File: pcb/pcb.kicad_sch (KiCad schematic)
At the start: 43 parts, among them J1 GND, J10 SWDIO, J11 SWCLK, J12 USART1 TX, J13 USART1 RX, J14 VDD, J2 +3.3V, J3 LCD Data, J4 LCD RS, J5 LCD E, J6 3.3v, J7 ADC2, J8 GND, J9 USART3 TX, P1 USB_C_Plug_USB2.0, U1 TLV62569DBV, U2 STM32F446RETx, U3 MCP73831-2-OT

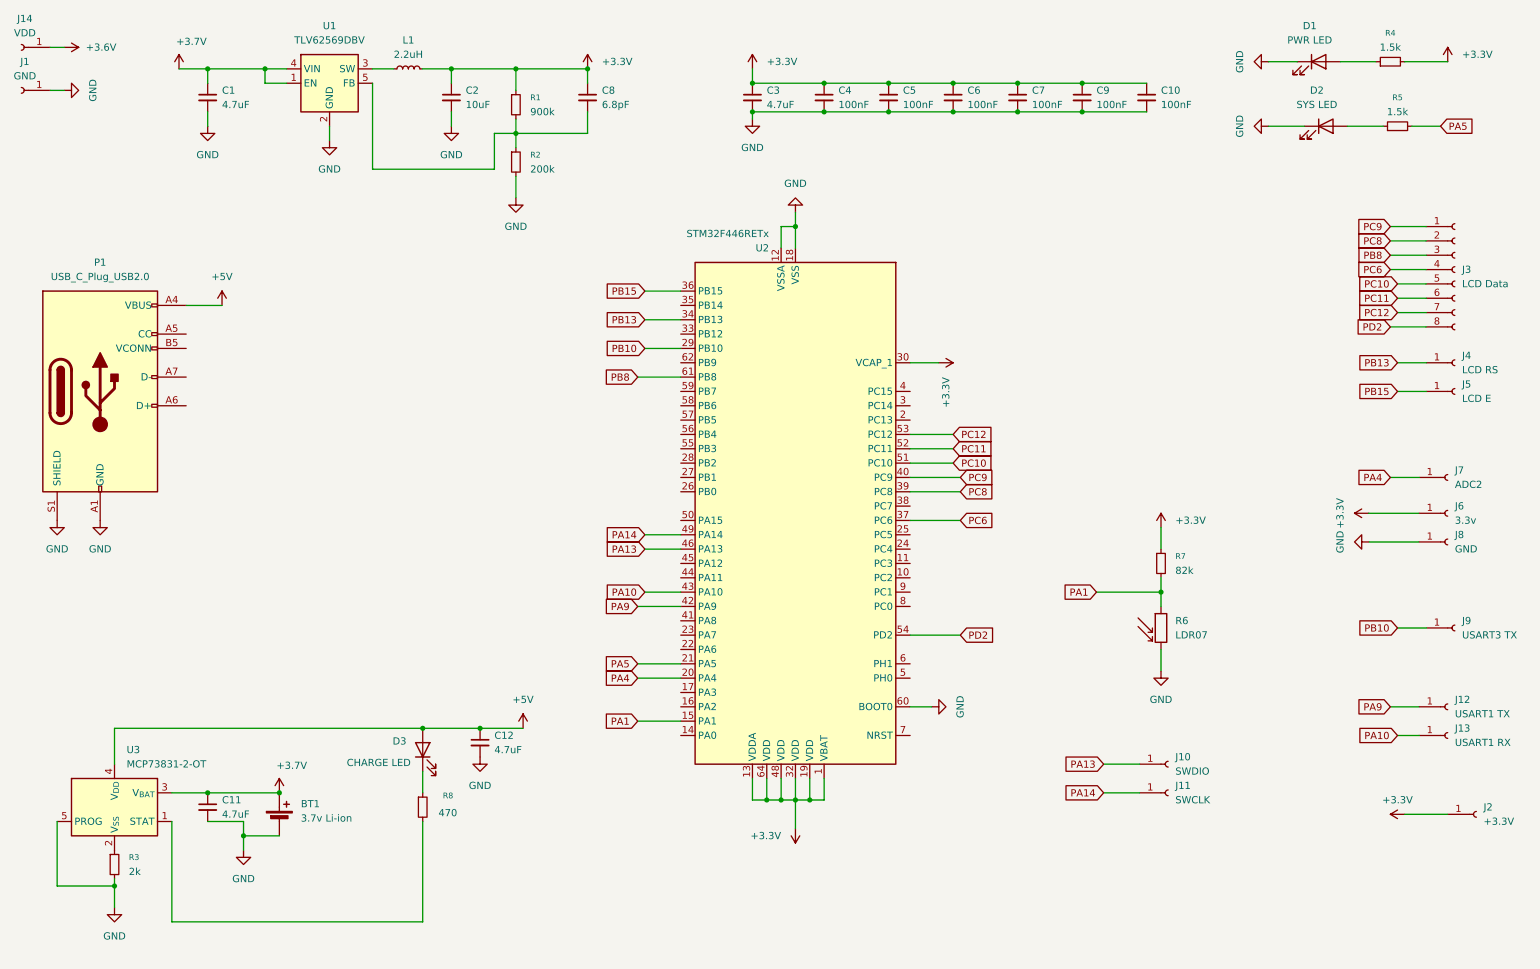
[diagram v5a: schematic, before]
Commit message: Add power and gnd pins for each component
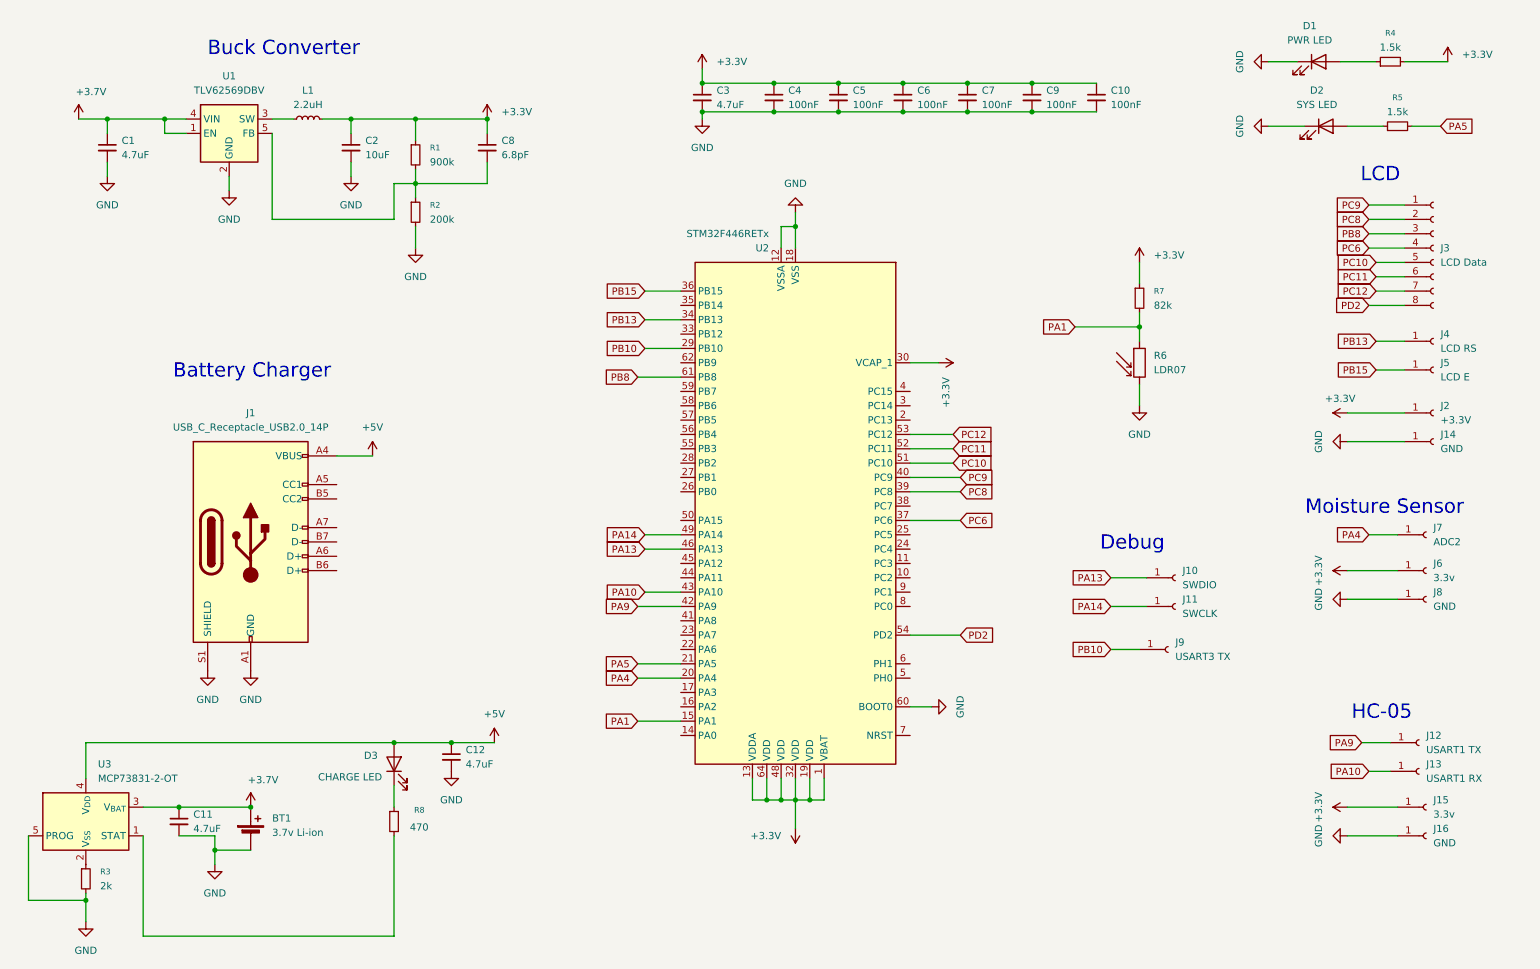
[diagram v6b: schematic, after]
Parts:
- removed J1: GND, symbol Connector:Conn_01x01_Socket
- removed P1: USB_C_Plug_USB2.0, symbol Connector:USB_C_Plug_USB2.0
- added J1: USB_C_Receptacle_USB2.0_14P, symbol Connector:USB_C_Receptacle_USB2.0_14P
- added J15: 3.3v, symbol Connector:Conn_01x01_Socket
- added J16: GND, symbol Connector:Conn_01x01_Socket
- J14: value VDD -> GND
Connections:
- net +3.6V is gone; now on net GND: J14.1 (Pin_1)
- net +3.3V: now also J15.1 (Pin_1)
- net +5V: now also J1.A4 (VBUS), J1.A9 (VBUS), J1.B4 (VBUS), J1.B9 (VBUS)
- net GND: now also J1.A1 (GND), J1.A12 (GND), J1.B1 (GND), J1.B12 (GND), J1.S1 (SHIELD), J16.1 (Pin_1)
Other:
- note added: "Battery Charger"
- note added: "Buck Converter"
- note added: "Debug"
- note added: "HC-05"
- note added: "LCD"
- note added: "Moisture Sensor"
- moved on the sheet: BT1, C1, C10, C11, C12, C2, C3, C4, C5, C6, C7, C8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

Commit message: small schematic tweaks
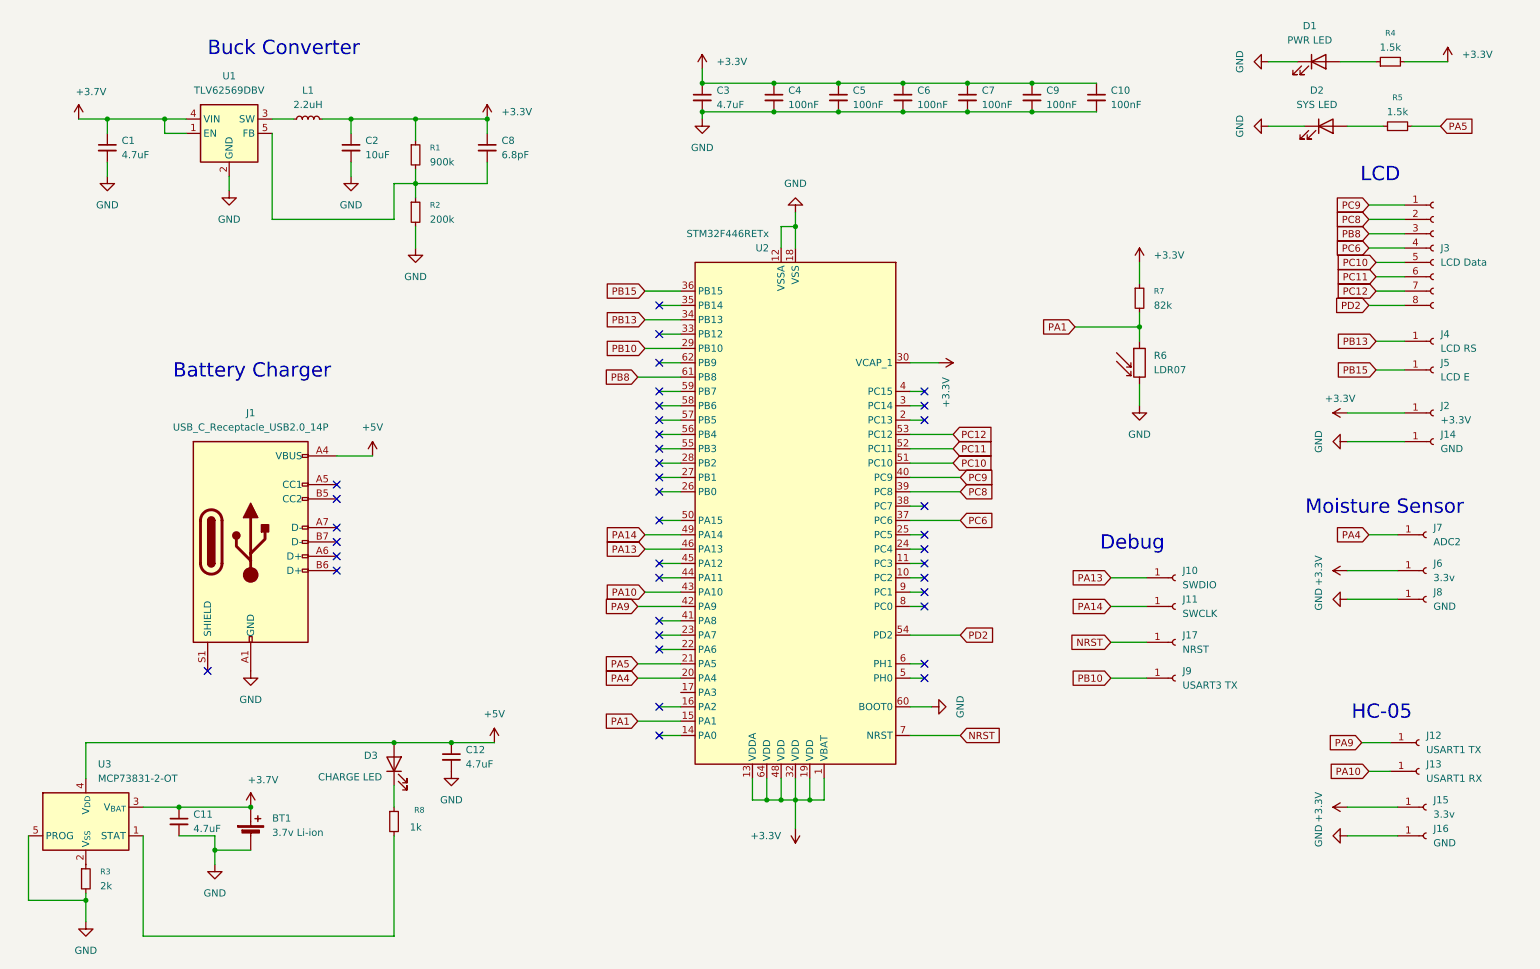
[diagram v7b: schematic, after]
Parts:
- added J17: NRST, symbol Connector:Conn_01x01_Socket
- R8: value 470 -> 1k
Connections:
- net GND: no longer J1.S1 (SHIELD)
- net NRST: now reaches U2.7 (NRST)
- net NRST: now also J17.1 (Pin_1)
- no-connect marks 0 -> 38
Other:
- moved on the sheet: J9

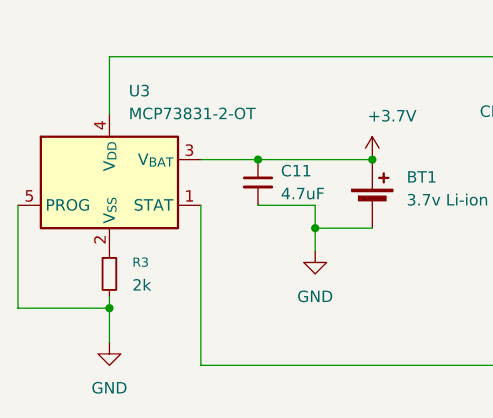
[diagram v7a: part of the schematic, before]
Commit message: fix charging circuit resistor
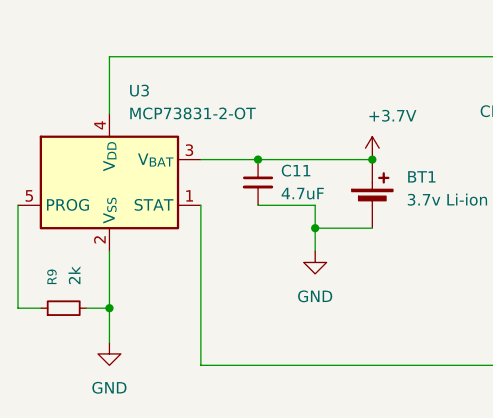
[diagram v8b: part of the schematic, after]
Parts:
- removed R3: 2k, symbol Device:R_Small
- added R9: 2k, symbol Device:R_Small
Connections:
- net GND: now also U3.2 (V_{SS}), R9.2; no longer U3.5 (PROG)
- new net: R9.1, U3.5 (PROG)
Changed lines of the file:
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@@
 	)
 	(junction
-		(at 27.94 172.72)
-		(diameter 0)
-		(color 0 0 0 0)
-	)
-	(junction
 		(at 41.91 34.29)
 		(diameter 0)
@@
 	)
 	(junction
+		(at 27.94 172.72)
+		(diameter 0)
+		(color 0 0 0 0)
+	)
+	(junction
 		(at 172.72 33.02)
 		(diameter 0)
@@
 	(wire
 		(pts
+			(xy 17.78 172.72) (xy 20.32 172.72)
+		)
+		(stroke
+			(width 0)
+			(type default)
+		)
+	)
+	(wire
+		(pts
 			(xy 133.35 64.77) (xy 127 64.77)
 		)
@@
 	(wire
 		(pts
-			(xy 27.94 172.72) (xy 27.94 176.53)
-		)
-		(stroke
-			(width 0)
-			(type default)
-		)
-	)
-	(wire
-		(pts
 			(xy 82.55 144.78) (xy 92.71 144.78)
 		)
@@
 	(wire
 		(pts
-			(xy 17.78 172.72) (xy 27.94 172.72)
+			(xy 129.54 85.09) (xy 133.35 85.09)
 		)
 		(stroke
@@
 	(wire
 		(pts
-			(xy 129.54 85.09) (xy 133.35 85.09)
+			(xy 251.46 86.36) (xy 261.62 86.36)
 		)
 		(stroke
@@
 	(wire
 		(pts
-			(xy 251.46 86.36) (xy 261.62 86.36)
+			(xy 129.54 128.27) (xy 133.35 128.27)
 		)
 		(stroke
@@
 	(wire
 		(pts
-			(xy 129.54 128.27) (xy 133.35 128.27)
+			(xy 69.85 34.29) (xy 74.93 34.29)
 		)
 		(stroke
@@
 	(wire
 		(pts
-			(xy 69.85 34.29) (xy 74.93 34.29)
+			(xy 256.54 62.23) (xy 261.62 62.23)
 		)
 		(stroke
@@
 	(wire
 		(pts
-			(xy 256.54 62.23) (xy 261.62 62.23)
+			(xy 129.54 95.25) (xy 133.35 95.25)
 		)
 		(stroke
@@
 	(wire
 		(pts
-			(xy 129.54 95.25) (xy 133.35 95.25)
+			(xy 129.54 100.33) (xy 133.35 100.33)
 		)
 		(stroke
@@
 	(wire
 		(pts
-			(xy 129.54 100.33) (xy 133.35 100.33)
+			(xy 27.94 172.72) (xy 27.94 176.53)
 		)
 		(stroke
@@
 	(wire
 		(pts
-			(xy 27.94 172.72) (xy 27.94 171.45)
-		)
-		(stroke
-			(width 0)
-			(type default)
-		)
-	)
-	(wire
-		(pts
 			(xy 255.27 49.53) (xy 261.62 49.53)
 		)
@@
 	(wire
 		(pts
+			(xy 25.4 172.72) (xy 27.94 172.72)
+		)
+		(stroke
+			(width 0)
+			(type default)
+		)
+	)
+	(wire
+		(pts
+			(xy 27.94 166.37) (xy 27.94 172.72)
+		)
+		(stroke
+			(width 0)
+			(type default)
+		)
+	)
+	(wire
+		(pts
 			(xy 215.9 120.65) (xy 209.55 120.65)
 		)
@@
 	)
 	(symbol
+		(lib_id "Device:R_Small")
+		(at 22.86 172.72 90)
+		(unit 1)
+		(exclude_from_sim no)
+		(in_bom yes)
+		(on_board yes)
+		(dnp no)
+		(fields_autoplaced yes)
+		(property "Reference" "R9"
+			(at 21.5899 170.18 0)
+			(effects
+				(font
+					(size 1.016 1.016)
+				)
+				(justify left)
+			)
+		)
+		(property "Value" "2k"
+			(at 24.1299 170.18 0)
+			(effects
+				(font
+					(size 1.27 1.27)
+				)
+				(justify left)
+			)
+		)
+		(property "Footprint" ""
+			(at 22.86 172.72 0)
+			(effects
+				(font
+					(size 1.27 1.27)
+				)
+				(hide yes)
+			)
+		)
+		(property "Datasheet" "~"
+			(at 22.86 172.72 0)
+			(effects
+				(font
+					(size 1.27 1.27)
+				)
+				(hide yes)
+			)
+		)
+		(property "Description" "Resistor, small symbol"
+			(at 22.86 172.72 0)
+			(effects
+				(font
+					(size 1.27 1.27)
+				)
+				(hide yes)
+			)
+		)
+		(pin "2"
+		)
+		(pin "1"
+		)
+		(instances
+			(project "pcb"
+				(path "/a02550bc-85b4-480d-868d-ccdfd0f6046d"
+					(reference "R9")
+					(unit 1)
+				)
+			)
+		)
+	)
+	(symbol
 		(lib_id "Connector:Conn_01x01_Socket")
 		(at 265.43 114.3 0)
@@
 	)
 	(symbol
-		(lib_id "Device:R_Small")
-		(at 27.94 168.91 0)
-		(unit 1)
-		(exclude_from_sim no)
-		(in_bom yes)
-		(on_board yes)
-		(dnp no)
-		(fields_autoplaced yes)
-		(property "Reference" "R3"
-			(at 30.48 167.6399 0)
-			(effects
-				(font
-					(size 1.016 1.016)
-				)
-				(justify left)
-			)
-		)
-		(property "Value" "2k"
-			(at 30.48 170.1799 0)
-			(effects
-				(font
-					(size 1.27 1.27)
-				)
-				(justify left)
-			)
-		)
-		(property "Footprint" ""
-			(at 27.94 168.91 0)
-			(effects
-				(font
-					(size 1.27 1.27)
-				)
-				(hide yes)
-			)
-		)
-		(property "Datasheet" "~"
-			(at 27.94 168.91 0)
-			(effects
-				(font
-					(size 1.27 1.27)
-				)
-				(hide yes)
-			)
-		)
-		(property "Description" "Resistor, small symbol"
-			(at 27.94 168.91 0)
-			(effects
-				(font
-					(size 1.27 1.27)
-				)
-				(hide yes)
-			)
-		)
-		(pin "2"
-		)
-		(pin "1"
-		)
-		(instances
-			(project ""
-				(path "/a02550bc-85b4-480d-868d-ccdfd0f6046d"
-					(reference "R3")
-					(unit 1)
-				)
-			)
-		)
-	)
-	(symbol
 		(lib_id "power:GND")
 		(at 92.71 149.86 0)
@@
 					(size 1.27 1.27)
 				)
-				(hide yes)
 			)
 		)
